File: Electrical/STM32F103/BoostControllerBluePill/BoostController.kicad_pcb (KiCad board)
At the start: 2 copper layers, 81.8 x 80 mm, 62 parts, among them J1 PW-RPM-SPD-TPS, J2 OIL-WATER-AFR, J3 WG-FPUMP, J4 MAP-FPRES, J5 CAN, J6 GND_TP, J7 PROG, Q1 IRF3205, Q2 IRF3205, Q3 S9013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

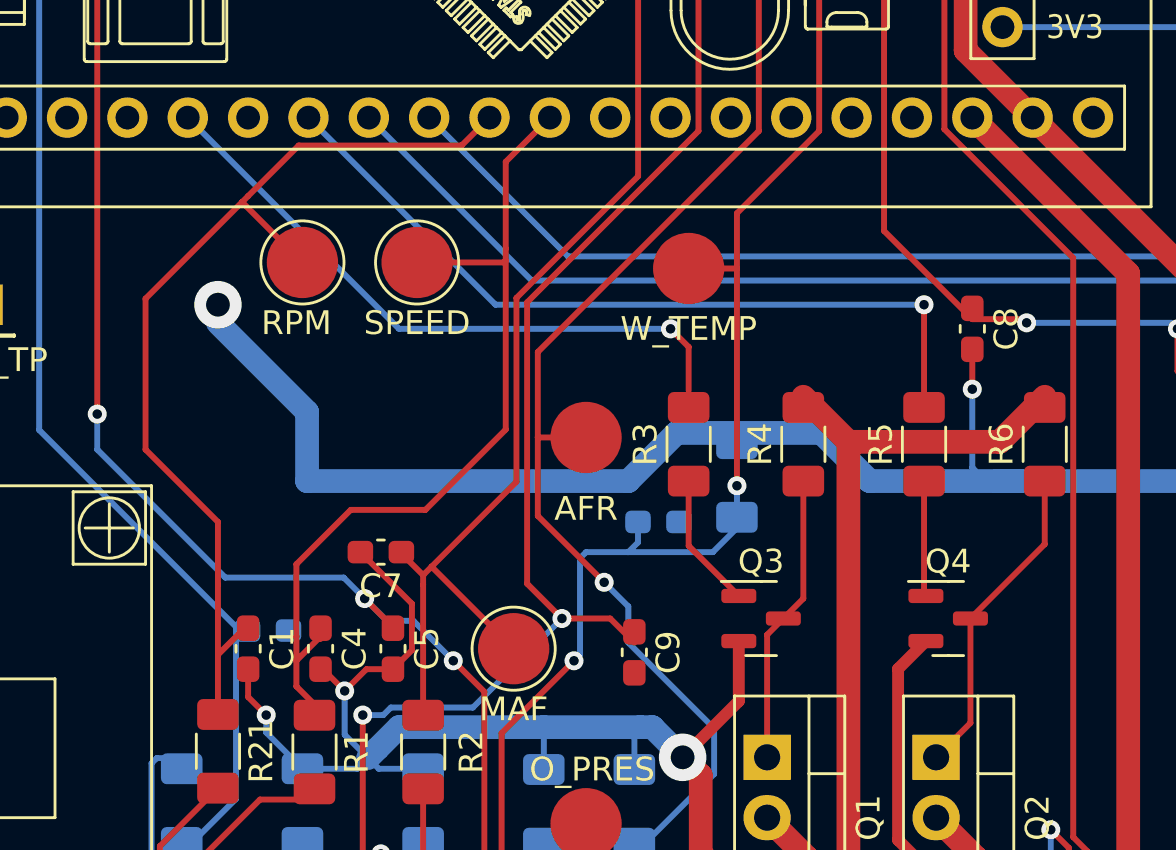
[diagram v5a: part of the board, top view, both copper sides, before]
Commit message: [Electrical] Changed  frequency input voltage divider + filter rather than zener diode clamping.
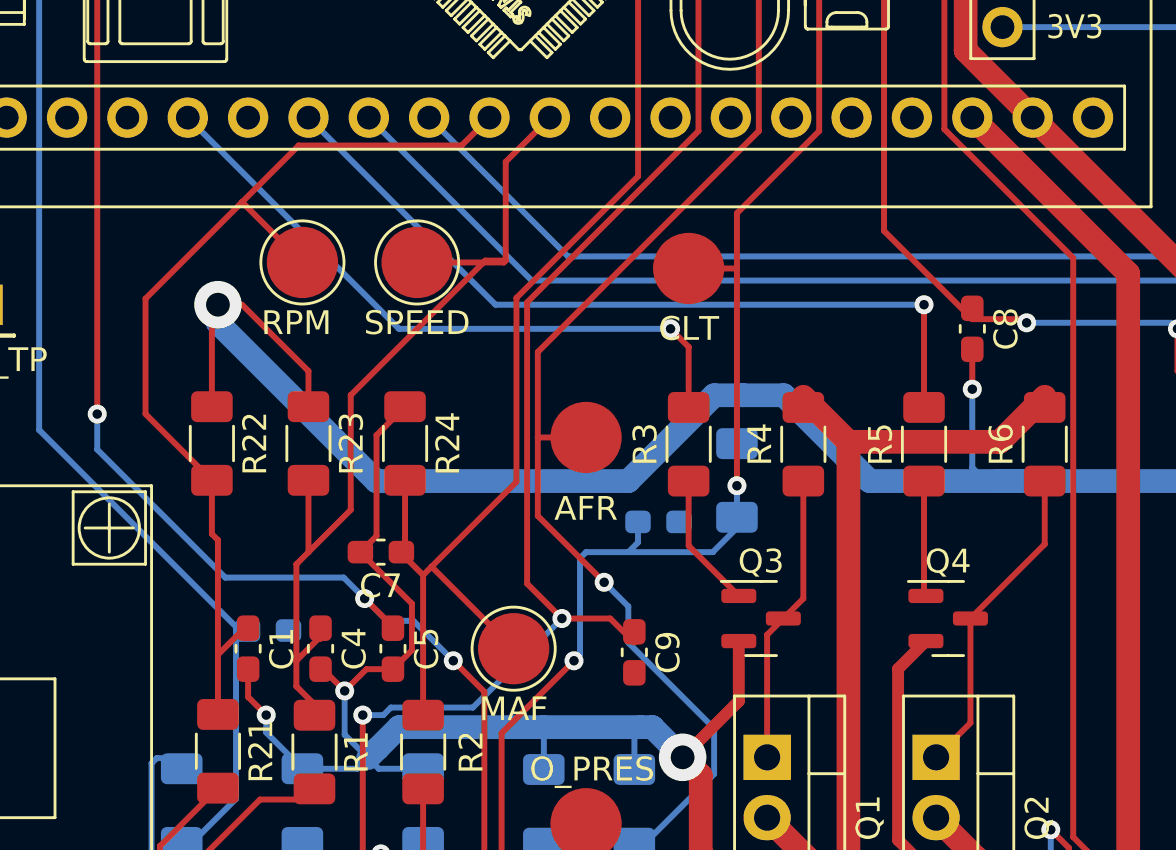
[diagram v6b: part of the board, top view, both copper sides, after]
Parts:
- added R22: 2.2k, Resistor_SMD:R_1206_3216Metric_Pad1.30x1.75mm_HandSolder, F.Cu at (75.9, 83.1)
- added R23: 2.2k, Resistor_SMD:R_1206_3216Metric_Pad1.30x1.75mm_HandSolder, F.Cu at (80.0, 83.1)
- added R24: 2.2k, Resistor_SMD:R_1206_3216Metric_Pad1.30x1.75mm_HandSolder, F.Cu at (84.1, 83.1)
- R1, R2, R21: value 4.7k -> 1.2k
- TP3: value W_TEMP -> CLT
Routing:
- net GND: track 421.9 -> 442.7 mm
- net /MAF_33: track 65.2 -> 68.3 mm
- net /SPEED_33: track 36.4 -> 38.1 mm

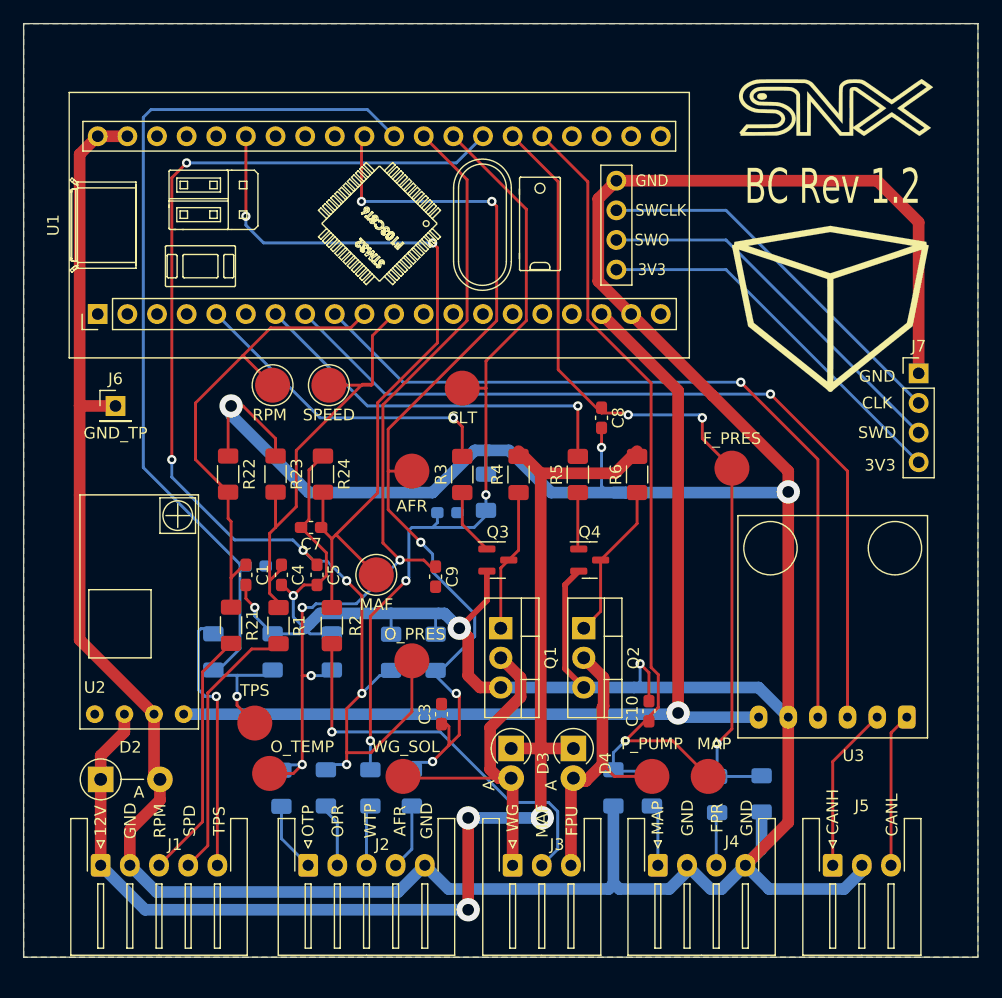
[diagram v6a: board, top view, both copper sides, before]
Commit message: Added serial port support on dupond header for local data logging. Added missing MAF input resistor. Changed power transistor reference. Changed analog input voltage divisor values.
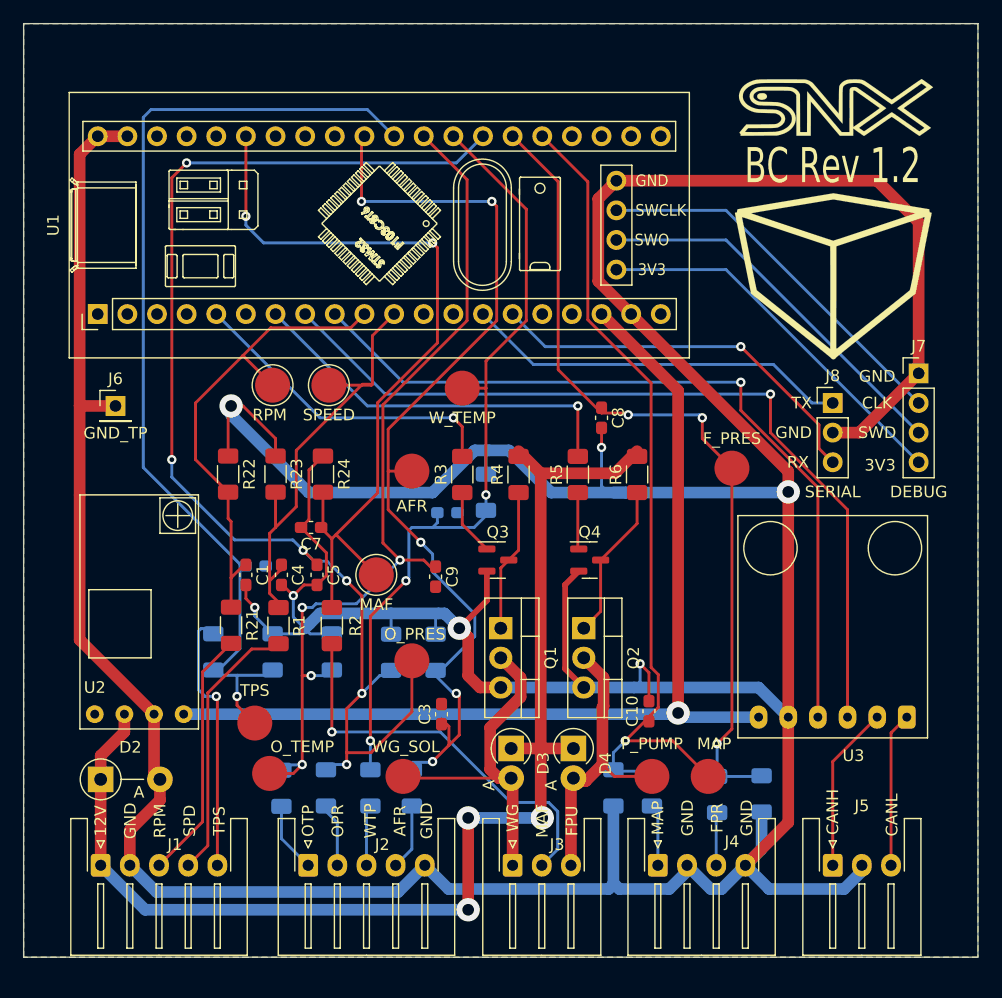
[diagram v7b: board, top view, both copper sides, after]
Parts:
- added J8: SERIAL, Connector_PinHeader_2.54mm:PinHeader_1x03_P2.54mm_Vertical, F.Cu at (127.8, 77.0)
- TP3: value CLT -> W_TEMP
- moved Ref** 2.81 mm to (128.0, 65.3)
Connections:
- U1 pad 14: unconnected-(U1-Pad14) -> /TX
- U1 pad 15: unconnected-(U1-Pad15) -> /RX
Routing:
- net /RX: track 0.00 -> 33.9 mm, vias 0 -> 1
- net /TX: track 0.00 -> 33.1 mm
- net GND: track 442.7 -> 452.2 mm
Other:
- board text added: "DEBUG"
- board text added: "RX"
- board text added: "SERIAL"
- board text added: "TX"
